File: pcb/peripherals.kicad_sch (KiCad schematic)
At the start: 0 parts

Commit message: Add symbol/footprint libraries and update peripherals.kicad_sch
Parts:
- added C17: 4.7 nF, Capacitor_SMD:C_0402_1005Metric_Pad0.74x0.62mm_HandSolder, symbol Device:C_Small
- added C18, C19: 100 pF, Capacitor_SMD:C_0402_1005Metric_Pad0.74x0.62mm_HandSolder, symbol Device:C_Small
- added C20, C?: 270nF ±10% X7R 0402, Capacitor_SMD:C_0402_1005Metric, symbol Device:C_Small
- added D? (x3): 5V, Diode_SMD:D_SOD-882, symbol Device:D_TVS_Small
- added D?: SM712-ES, Package_TO_SOT_SMD:SOT-23, symbol Diode:SM712_SOT23
- added D?: SK6812SMINI-ER, SK6812SMINI-ER:LED-SMD_4P-L3.5-W2.8-BR-1, symbol SK6812:SK6812
- added FL?: ACT45B-101-2P-TL003, ACT45B-101-2P-TL003:FILTER-SMD_4P-L4.5-W3.2-TL_ACT45B, symbol Filter:Choke_CommonMode_FerriteCore_1423
- added J?: TYPE-C 16PIN Vertical, TYPEC-303-ACP16:USB-C-SMD_TYPEC-303-ACP16, symbol Connector:USB_C_Receptacle_USB2.0_16P
- added R11, R12: 60Ω ±1%, Resistor_SMD:R_0402_1005Metric, symbol Device:R_Small_US
- added R? (x2): 5.1kΩ ±1%, Resistor_SMD:R_0402_1005Metric, symbol Device:R_Small_US
- added U?: TCAN332G, symbol Interface_CAN_LIN:TCAN332G
- added U?: SN74LV1T34DCK, Package_TO_SOT_SMD:SOT-353_SC-70-5, symbol Logic_LevelTranslator:SN74LV1T34DCK
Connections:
- new net: FL?.2, U?.6 (CANL)
- new net: FL?.1, U?.7 (CANH)
- new net: C17.1, R11.2, R12.1
- new net: J?.A5 (CC1), R?.1
- new net: J?.B5 (CC2), R?.1
- new net: D?.2 (DIN), U?.4 (Y)
- new net +3V3: C20.1, U?.3 (VCC)
- new net +5V: C?.1, D?.3 (VDD), U?.5 (VCC)
- new net +VUSB_PROG: D?.2 (A2), J?.A4 (VBUS), J?.A9 (VBUS), J?.B4 (VBUS), J?.B9 (VBUS)
- new net ARGB_DAT_5V: D?.4 (DOUT)
- new net CANH: C19.1, D?.2 (A2), FL?.4, R11.1
- new net CANL: C18.1, D?.1 (A1), FL?.3, R12.2
- new net CAN_RX: U?.4 (RXD)
- new net CAN_TX: U?.1 (TXD)
- new net GND: C17.2, C18.2, C19.2, C20.2, C?.2, D?.1 (A1), D?.1 (A1), D?.1 (A1), D?.1 (VSS), D?.3 (common), J?.A1 (GND), J?.A12 (GND), J?.B1 (GND), J?.B12 (GND), J?.S1 (SHIELD), R?.2, R?.2, U?.2 (GND), U?.3 (GND)
- new net STAT_ARGB_DAT_3V3: U?.2 (A)
- new net USB_D+: D?.2 (A2), J?.A6 (D+), J?.B6 (D+)
- new net USB_D-: D?.2 (A2), J?.A7 (D-), J?.B7 (D-)
- no-connect marks 0 -> 2
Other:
- note added: "CAN Transiever"
- note added: "Change to whatever we have"
- note added: "Connectors"
- note added: "Decide if we want to use"
- note added: "Place a cap maybe"
- note added: "Programming USB"
- note added: "Status ARGB LED"
- note added: "https://www.ti.com/lit/an/slla271/slla271.pdf"
- note added: "https://www.ti.com/lit/ug/sllu231/sllu231.pdf"

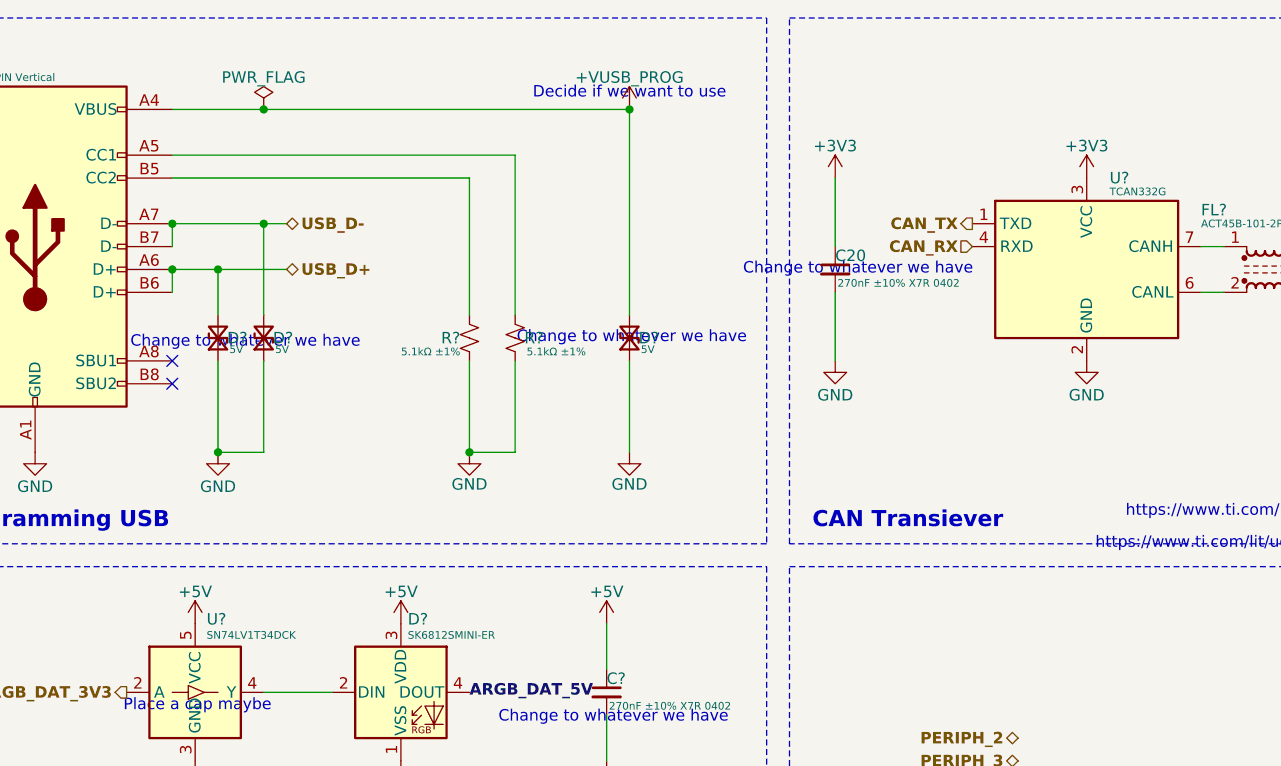
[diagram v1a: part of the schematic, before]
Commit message: Completed Initial Power Draft for Review, and Updated Flags
Included notes for review
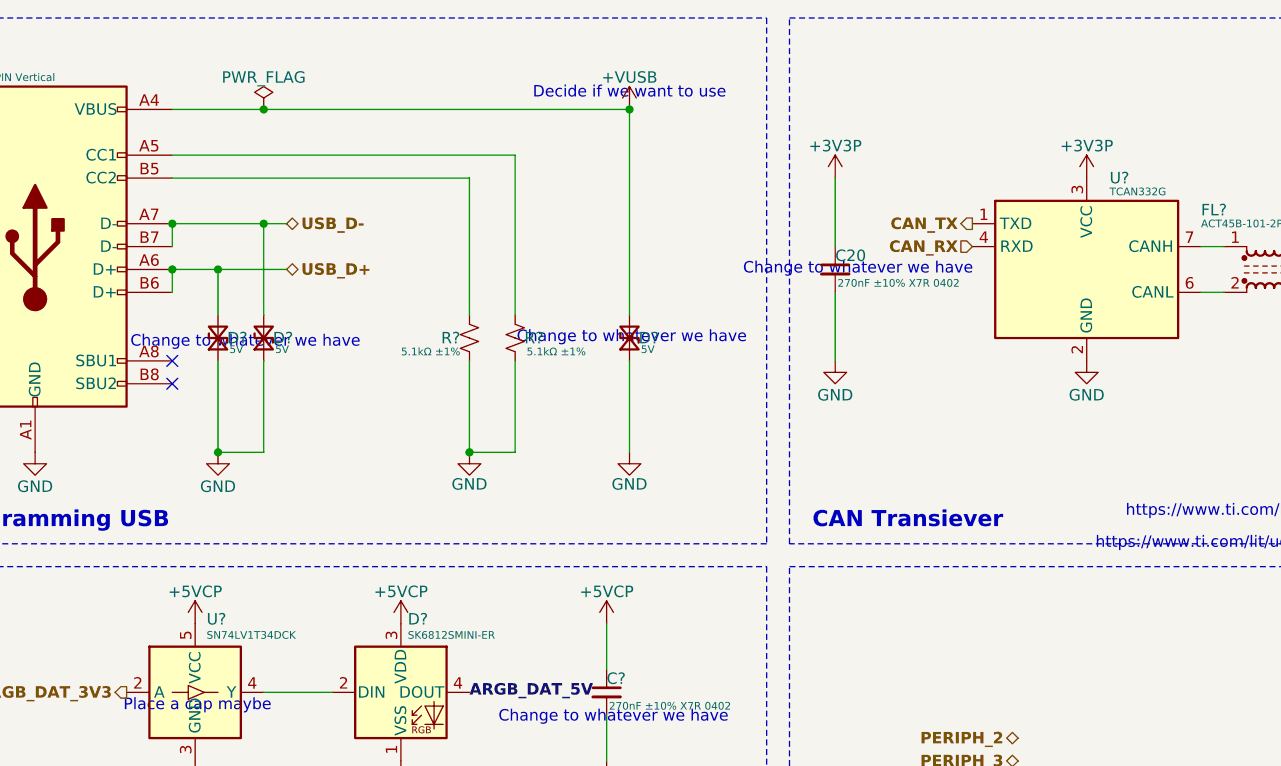
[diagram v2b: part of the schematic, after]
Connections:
- net +3V3 renamed +3V3P
- net +5V renamed +5VCP
- net +VUSB_PROG renamed +VUSB
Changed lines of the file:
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@@
 			"zfa7Q+POwHsLY9RhwMCHgu6uLjH1CKTNG1rUTh5PTi0vHzRVBgwYMGDAQEs45lpeo+YuzYUeB+aW"
 			"UDjNNeVyDJMfUlf6oNG4M/DewjjXYcCAAQMGDBgwYMCAgf2Fca7DgAEDBgwYMGDAgAED+wtj1GHA"
-			"gAEDBgwYMGDAgIH9hTHqMGDAgAEDBgwYMGDAwP7i/wI4aZK0YHMQvQAAAABJRU5ErkJggg=="
+			"gAEDBgwYMGDAgIH9hTHqMGDAgAEDBgwYMGDAwP7i/wI4aZK0YHMQvQAAAABJRU5ErkJgggAwAHEA"
+			"RgBaAEYAUwA5ADcARwArAFAAcQBzAHkAUABNAFYAWQBYAGkATwBDAGkAdABRAEQALwBTAEIAUwB3"
+			"AG4AWQA4AEUAeAAwADkAbABCAHcAZgBqAFIAUQAwAGcATQBVAFMAagBlAEcAeAB6AHEAQwBLACsA"
+			"SQBFAFAATQBoAFIAcwBuAGQAWQBCAG0AYgBCAHMAQwArAC8AOABuADAAWABnAGUARQA4ADYALwB0"
+			"ADMAUAAvAEgAVABvADYAaAB4AGMASwB5AHgAbQBNAE4AVAA4AHUAZQBrAFkAdgBPAE4ARABZAHoA"
+			"dQBQAGIAawBzAEMANgA0ADIARwBtAGEAawBMAG0ATAA3AEMAdwBIAEEAdwBBAHUAawBlAFUAOABI"
+			"AHUAWgBtAEkAQQBwADEARQBCADYAVABJAEEAZABvAGQAaQBSADQAUwBnAEMAVgBKAGMAMwBNAHUA"
+			"dwBhADQAMwBrAGQAeABFAEYARABsAEEAUgBtAEEAUAA4AHcASABQAEEAZABzAEIAZQA4AGoAZgBl"
+			"ADAANwBtAHIARABlAEwAVAA1AFUAVQAyAGUAUwBjAE4ANABYAFIAaABkAGoATQBTAGIAUABKAG0A"
+			"UQBsAHoAUQA5AEcAWgBZAGQAbQB4AEMATABKAFoATQAwAGgANAB5ADgAZwB1AHMAdAB5AGwAYgBz"
+			"ADcATgBjAFEAZgAzAFoAbQAxAFAAWgByAEkAWgBiAHkAYgBiAGsAeABhAEcATgBlAEsANQB1AGIA"
+			"ZQBsAFMAaABaAGkAQwBzAGYASgBsAEEALwBoAFcAbwA0AFoAaQB0AEkAaQB4AHUARgBsAHoAcwBY"
+			"AC8AUwBuAEcAZgB5AGUAYgBQAHgASABQADAAbQA2AEUAeABTAGYARQAzADUAdABLAEQAUgBPAFAA"
+			"agBhADAATQBWAFoAcAAvAGwAbQBPADkAWQBRAG8AawA4ADgAUgBQAFAAcABLADYAcgBwAEMANwBP"
+			"AGkANwA2AGQATwBSAEoAegBmAG4ARQBLAFEANAB6AEoAVwBOADAAWgB3AGcAZABCAFAATQBZAHMA"
+			"VABxADYANAB5AGkANABlAGkAcABoAEUARAAyAEgAeABmAE4AaQBnAGkAQwB0AHcASwBJADQAWgBN"
+			"AFMAOQAyAHgAegBHAEgARgBjAEkAUAAwAGUAVABrAFcAQQBnAGoAVgBiAE4AVwBPAFoAUgBTAEMA"
+			"YQB1ADIARQBNAEoAQQBvAGMASQB3AHoATQBNAE4AUwA4AGMARQBJAFEANgBMAE4ARgBtAFIAUQBp"
+			"AFIATQB6AEsAWgBoADIARABDAFUAaABsAG4ARABVAEEASwBwAE4AbwBNAEwAawBjAE0AMAAAAAAA"
+			"AAAAAAAAAAAAAAAAAAAAAAAAAAAAAAAAAAAAAAAAAAAAAAAAAAAAAAAAAAAAAAAAAAAAAAAAAAAA"
+			"AAAAAAAAAAAAAAAAAAAAAAAAAAAAAAAAAAAAAAAAAAAAAAAAAAAAAAAAAAAAAAAAAAAAAAAAAAAA"
+			"AAAAAAAAAAAAAAAAAAAAAAAAAAAAAAAAAAAAAAAAAAAAAAAAAAAAAAAAAAAAAAAAAAAAAAAAAAAA"
+			"AAAAAAAAAAAAAAAAAAAAAAAAAAAAAAAAAAAAAAAAAAAAAAAAAAAAAAAAAAAAAAAAAAAAAAAAAAAA"
+			"AAAAAAAAAAAAAAAAAAAAAAAAAAAAAAAAAAAAAAAAAAAAAAAAAAAAAAAAAAAAAAAAAAAAAAAAAAAA"
+			"AAAAAAAAAAAAAAAAAAAAAAAAAAAAAAAAAAAAAAAAAAAAAAAAAAAAAAAAAAAAAAAAAAAAAAAAAAAA"
+			"AAAAAAAAAAAAAAAAAAAAAAAAAAAAAAAAAAAAAAAAAAAAAAAAAAAAAAAAAAAAAAAAAAAAAAAAAAAA"
+			"AAAAAAAAAAAAAAAAAAAAAAAAAAAAAAAAAAAAAAAAAAAAAAAAAAAAAAAAAAAAAAAAAAAAAAAAAAAA"
+			"AAAAAAAAAAAAAAAAAAAAAAAAAAAAAAAAAAAAAAAAAAAAAAAAAAAAAAAAAAAAAAAAAAAAAAAAAAAA"
+			"AAAAAAAAAAAAAAAAAAAAAAAAAAAAAAAAAAAAAAAAAAAAAAAAAAAAAAAAAAAAAAAAAAAAAAAAAAAA"
+			"AAAAAAAAAAAAAAAAAAAAAAAAAAAAAAAAAAAAAAAAAAAAAAAAAAAAAAAAAAAAAAAAAAAAAAAAAAAA"
+			"AAAAAAAAAAAAAAAAAAAAAAAAAAAAAAAAAAAAAAAAAAAAAAAAAAAAAAAAAAAAAAAAAAAAAAAAAAAA"
+			"AAAAAAAAAAAAAAAAAAAAAAAAAAAAAAAAAAAAAAAAAAAAAAAAAAAAAAAAAAAAAAAAAAAAAAAAAAAA"
+			"AAAAAAAAAAAAAAAAAAAAAAAAAAAAAAAAAAAAAAAAAAAAAAAAAAAAAAAAAAAAAAAAAAAAAAAAAAAA"
+			"AAAAAAAAAAAAAAAAAAAAAAAAAAAAAAAAAAAAAAAAAAAAAAAAAAAAAAAAAAAAAAAAAAAAAAAAAAAA"
+			"AAAAAAAAAAAAAAAAAAAAAAAAAAAAAAAAAAAAAAAAAAAAAAAAAAAAAAAAAAAAAAAAAAAAAAAAAAAA"
+			"AAAAAAAAAAAAAAAAAAAAAAAAAAAAAAAAAAAAAAAAAAAAAAAAAAAAAAAAAAAAAAAAAAAAAAAAAAAA"
+			"AAAAAAAAAAAAAAAAAAAAAAAAAAAAAAAAAAAAAAAAAAAAAAAAAAAAAAAAAAAAAAAAAAAAAA=="
 		)
 	)
@@
 			)
 		)
-		(property "Value" "+VUSB_PROG"
+		(property "Value" "+VUSB"
 			(at 91.44 19.304 0)
 			(effects
@@
 			)
 		)
-		(property "Value" "+3V3"
+		(property "Value" "+3V3P"
 			(at 114.3 26.924 0)
 			(effects
@@
 			)
 		)
-		(property "Value" "+3V3"
+		(property "Value" "+3V3P"
 			(at 142.24 26.924 0)
 			(effects
@@
 			)
 		)
-		(property "Value" "+5V"
+		(property "Value" "+5VCP"
 			(at 66.04 76.454 0)
 			(effects
@@
 			)
 		)
-		(property "Value" "+5V"
+		(property "Value" "+5VCP"
 			(at 88.9 76.454 0)
 			(effects
@@
 			)
 		)
-		(property "Value" "+5V"
+		(property "Value" "+5VCP"
 			(at 43.18 76.454 0)
 			(effects

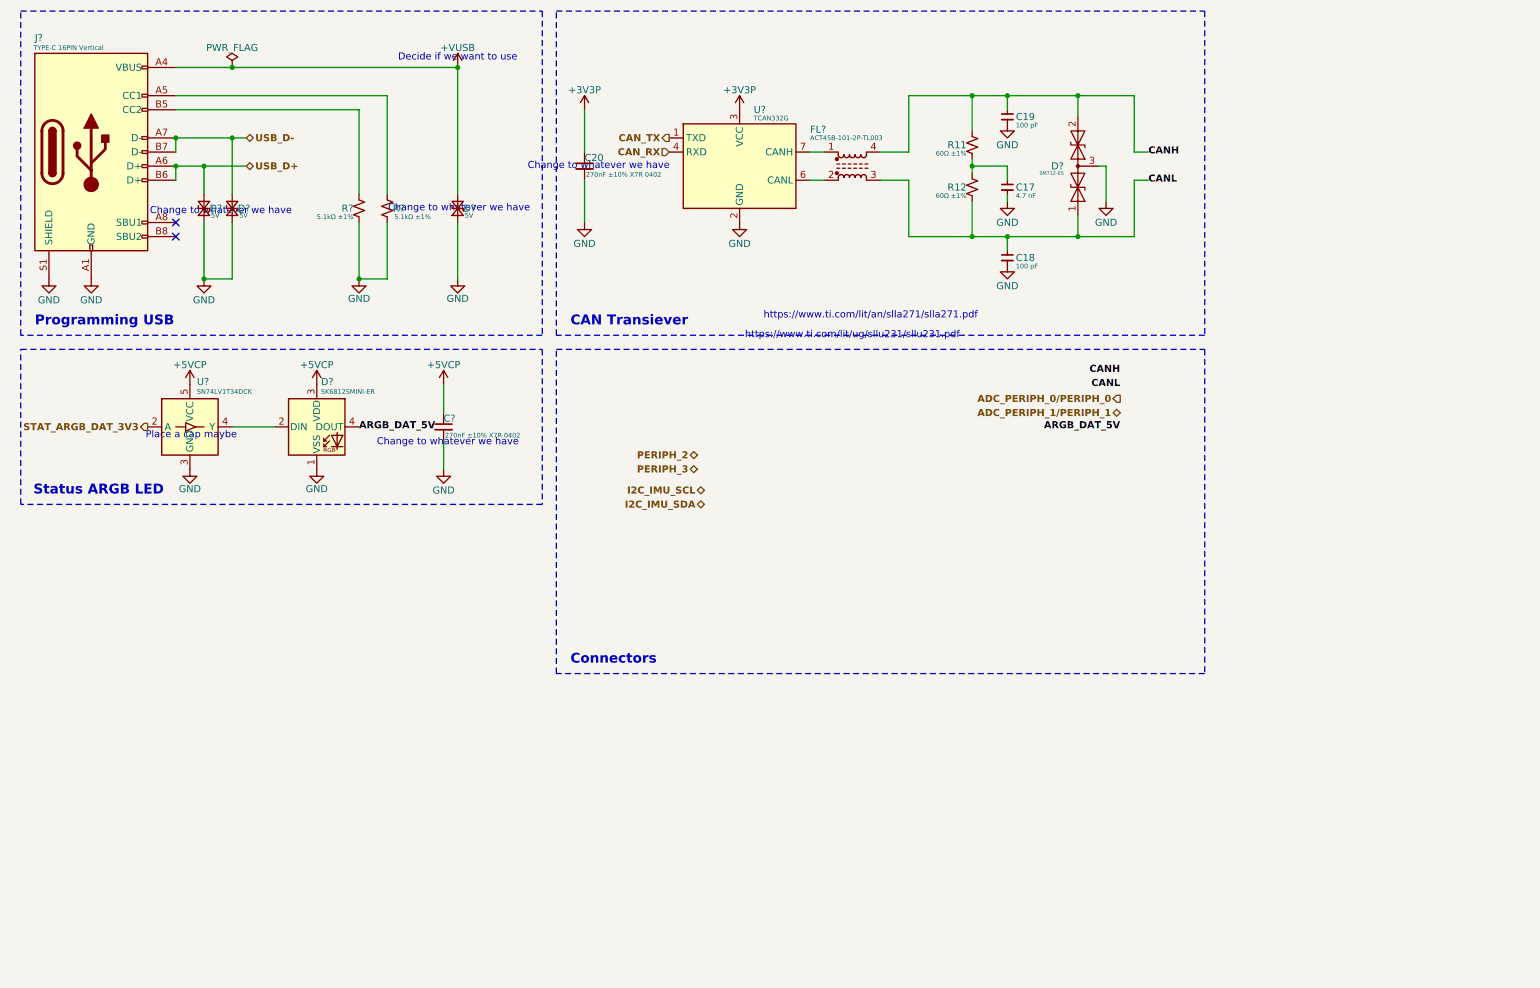
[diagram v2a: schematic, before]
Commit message: Updating label direction, added more info on io
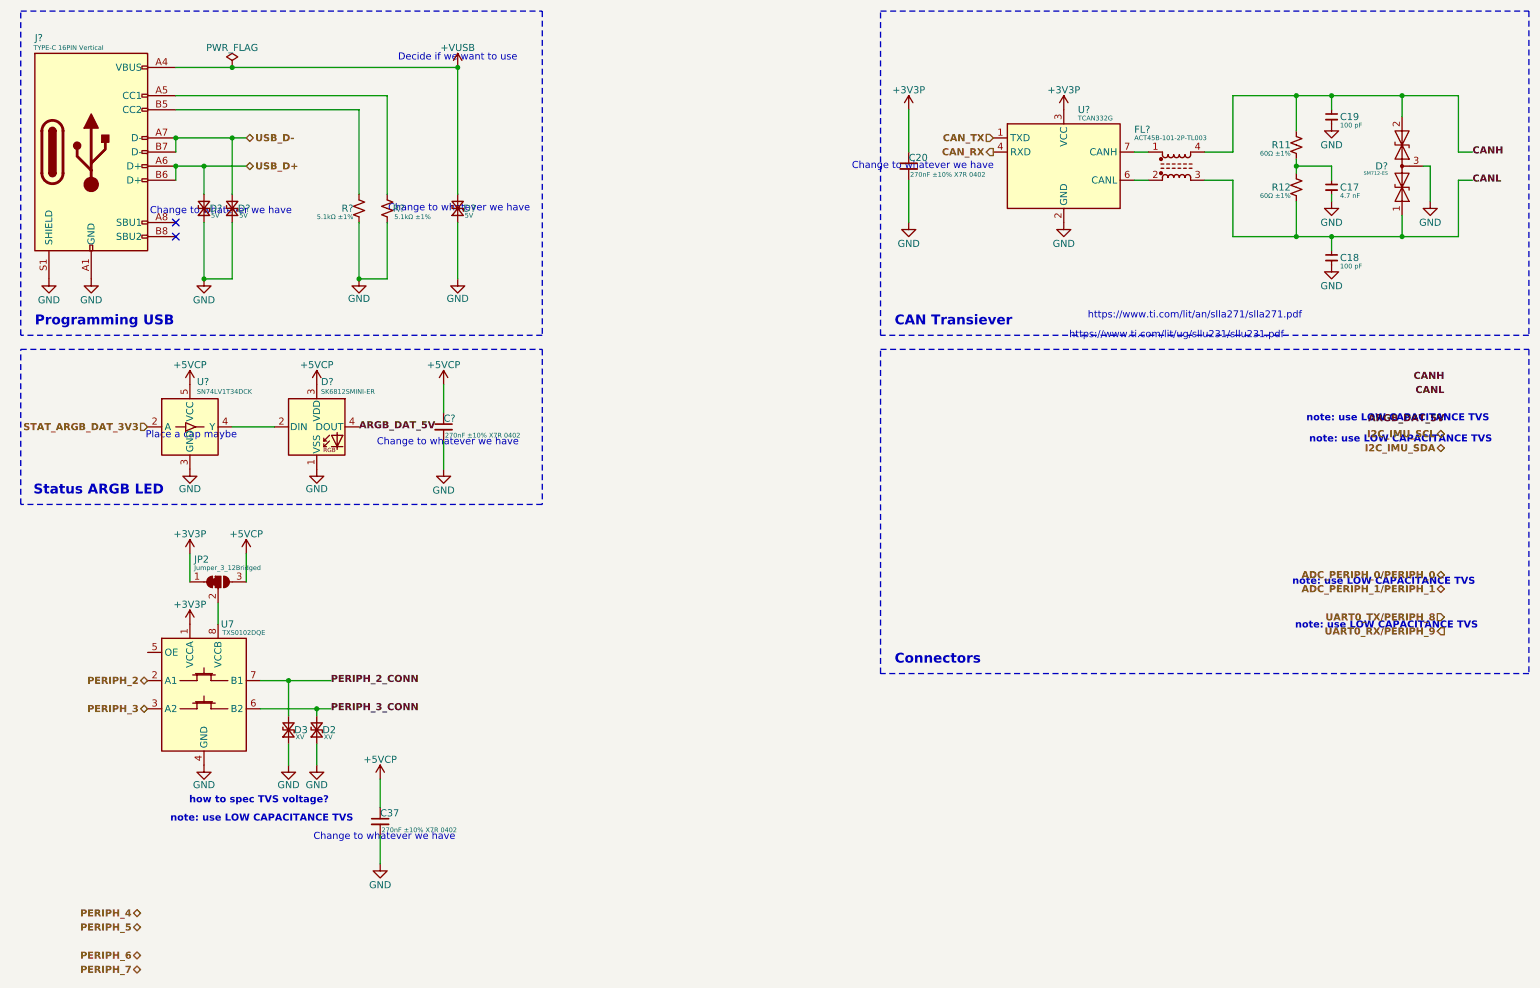
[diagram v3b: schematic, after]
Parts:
- added C37: 270nF ±10% X7R 0402, Capacitor_SMD:C_0402_1005Metric, symbol Device:C_Small
- added D2, D3: XV, symbol Device:D_TVS_Small
- added JP2: Jumper_3_12Bridged, Jumper:SolderJumper-3_P1.3mm_Bridged12_RoundedPad1.0x1.5mm, symbol Jumper:SolderJumper_3_Bridged12
- added U7: TXS0102DQE, Package_SON:X2SON-8_1.4x1mm_P0.35mm, symbol Logic_LevelTranslator:TXS0102DQE
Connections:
- net +3V3P: now also JP2.1 (A), U7.1 (VCCA)
- net +5VCP: now also C37.1, JP2.3 (B)
- net GND: now also C37.2, D2.1 (A1), D3.1 (A1), U7.4 (GND)
- net PERIPH_2: now also U7.2 (A1)
- net PERIPH_3: now also U7.3 (A2)
- new net: JP2.2 (C), U7.8 (VCCB)
- new net PERIPH_2_CONN: D3.2 (A2), U7.7 (B1)
- new net PERIPH_3_CONN: D2.2 (A2), U7.6 (B2)
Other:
- note added: "how to spec TVS voltage?"
- note added: "note: use LOW CAPACITANCE TVS"
- moved on the sheet: C17, C18, C19, C20, D?, FL?, R11, R12, U?

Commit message: Made updates to the power and driver sheet
Fixed converters and added motor connector
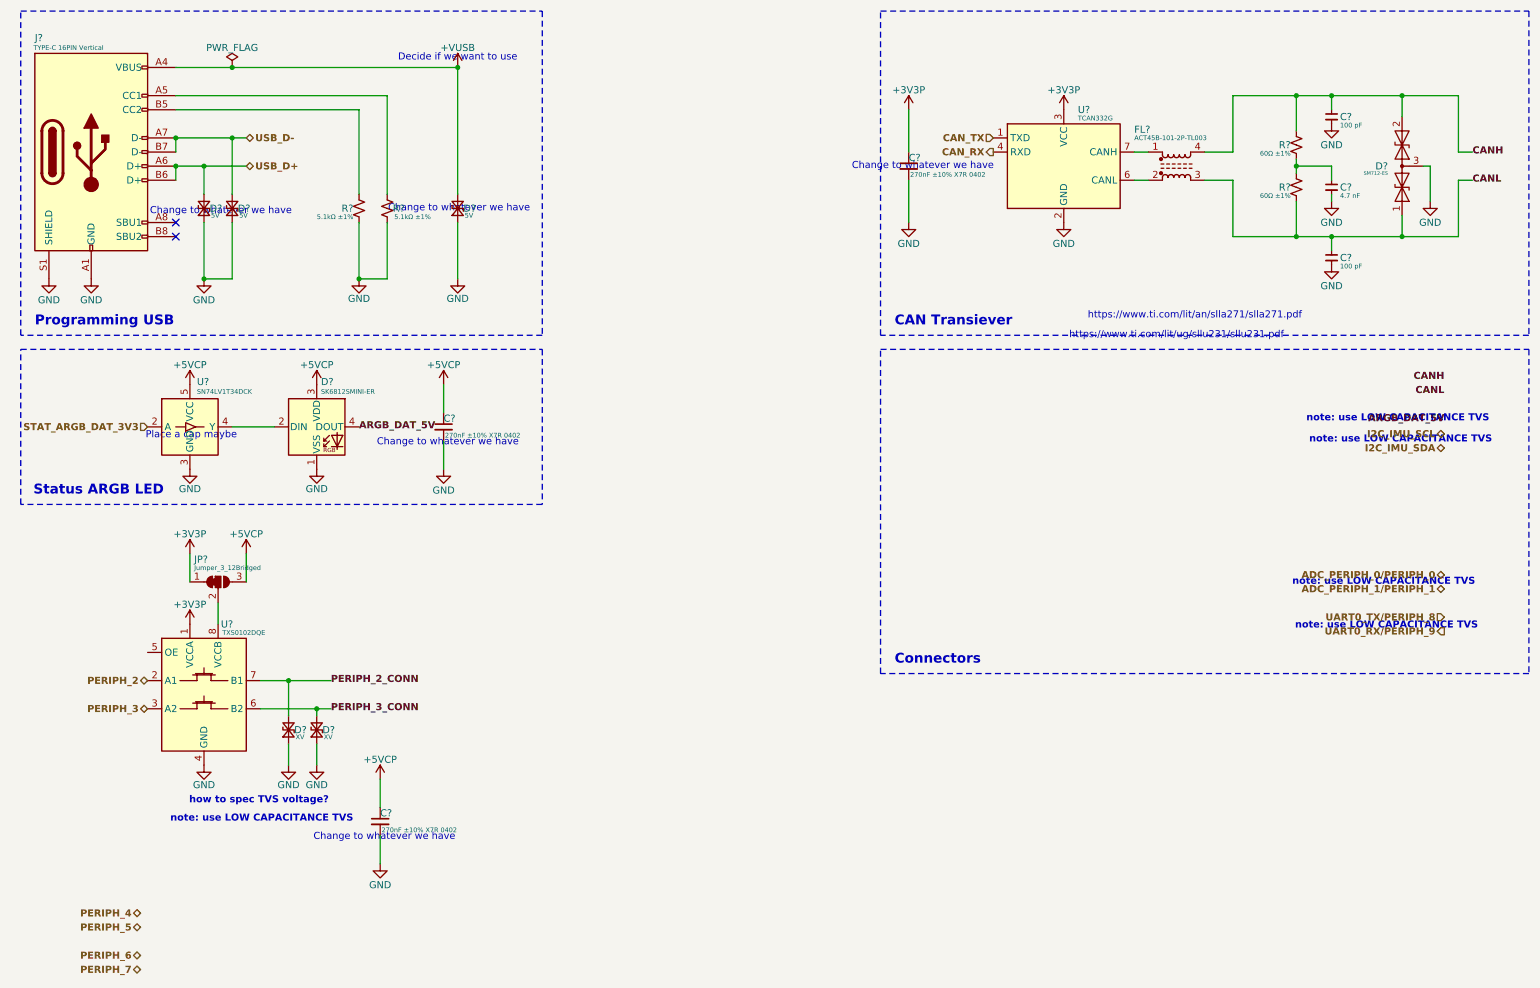
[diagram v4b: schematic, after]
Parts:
- renumbered C17 to C?, C37 to C?, C19 to C?, C18 to C?, C20 to C?, D3 to D?, D2 to D?, JP2 to JP?, R12 to R?, R11 to R?, U7 to U?
